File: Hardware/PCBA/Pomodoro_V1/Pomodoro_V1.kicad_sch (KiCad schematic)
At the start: 0 parts

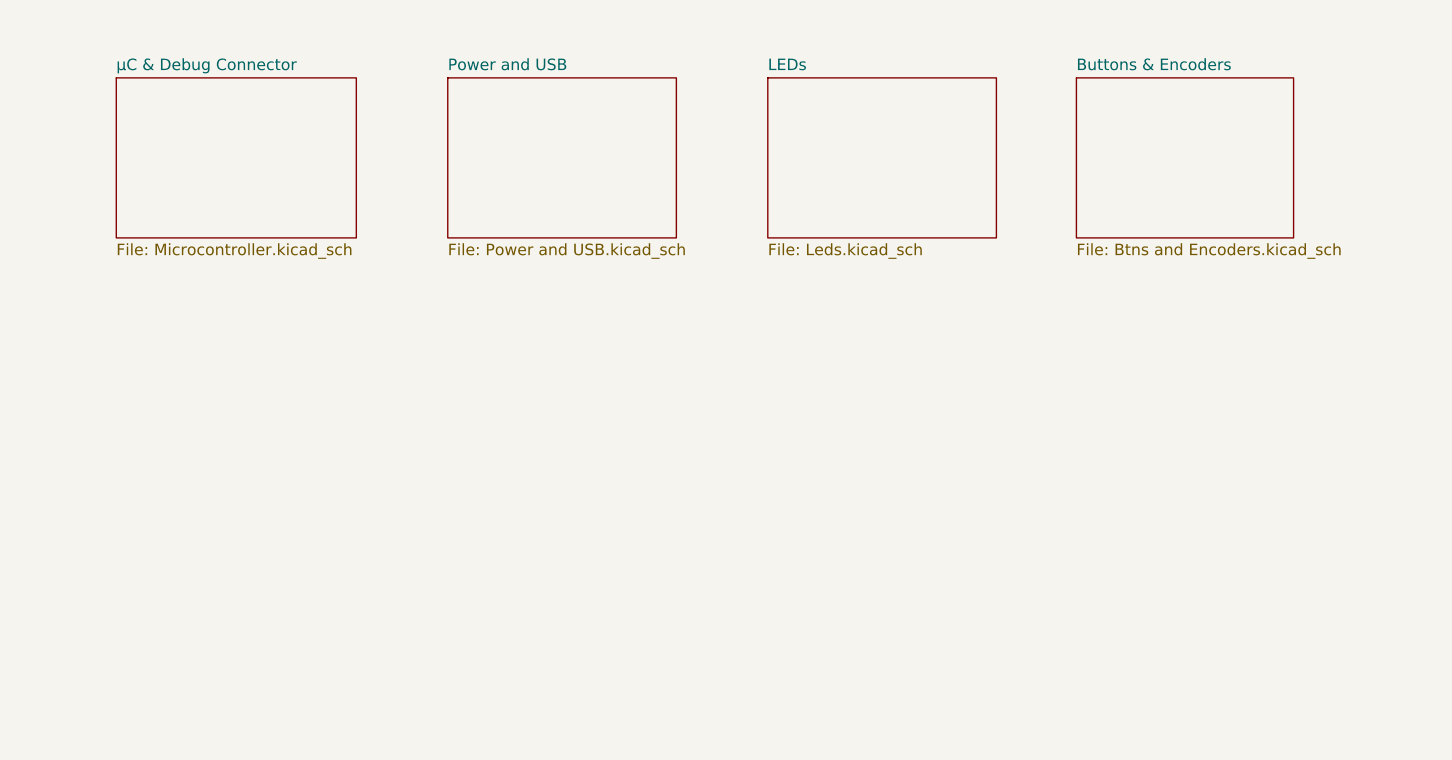
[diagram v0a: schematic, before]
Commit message: Updated CubeMx File, Created Schematic for µC, layouted the LEDs on the PCB
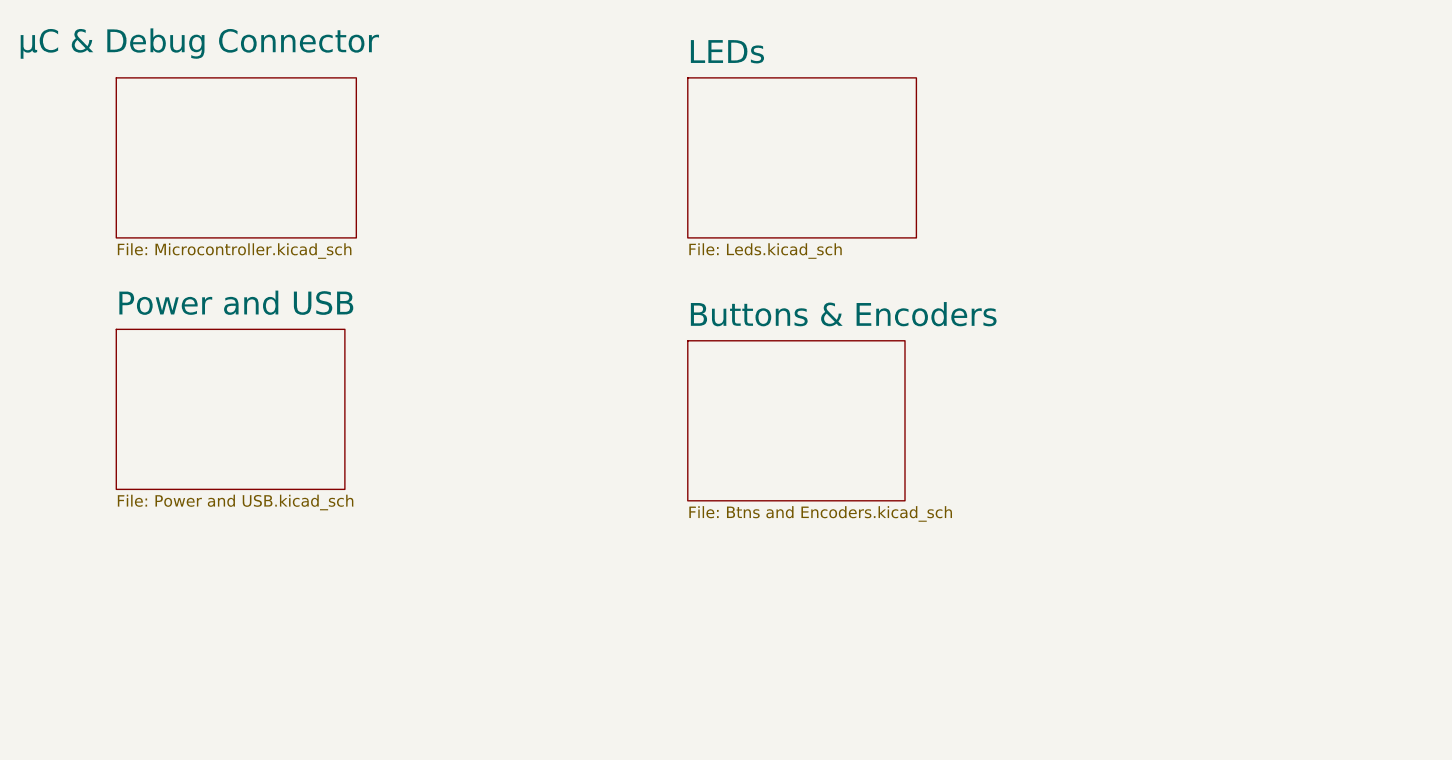
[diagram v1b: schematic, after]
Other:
- company: (none) -> Max Koell (c)
- title: (none) -> Pomodoro_Clock
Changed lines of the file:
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@@
 	(generator_version "8.0")
 	(paper "A4")
+	(title_block
+		(title "Pomodoro_Clock")
+		(date "2024-02-29")
+		(rev "1")
+		(company "Max Koell (c)")
+	)
 	(sheet
-		(at 134.62 63.5)
+		(at 125.73 63.5)
 		(size 25.4 17.78)
 		(fields_autoplaced yes)
@@
 		)
 		(property "Sheetname" "LEDs"
-			(at 134.62 62.7884 0)
+			(at 125.73 62.1534 0)
 			(effects
 				(font
-					(size 1.27 1.27)
+					(size 2.54 2.54)
 				)
 				(justify left bottom)
@@
 		)
 		(property "Sheetfile" "Leds.kicad_sch"
-			(at 134.62 81.8646 0)
+			(at 125.73 81.8646 0)
 			(effects
 				(font
@@
 		(at 62.23 63.5)
 		(size 26.67 17.78)
-		(fields_autoplaced yes)
 		(stroke
 			(width 0.1524)
@@
 		)
 		(property "Sheetname" "µC & Debug Connector"
-			(at 62.23 62.7884 0)
+			(at 51.308 60.96 0)
 			(effects
 				(font
-					(size 1.27 1.27)
+					(size 2.54 2.54)
 				)
 				(justify left bottom)
@@
 	)
 	(sheet
-		(at 168.91 63.5)
+		(at 125.73 92.71)
 		(size 24.13 17.78)
 		(fields_autoplaced yes)
@@
 		)
 		(property "Sheetname" "Buttons & Encoders"
-			(at 168.91 62.7884 0)
+			(at 125.73 91.3634 0)
 			(effects
 				(font
-					(size 1.27 1.27)
+					(size 2.54 2.54)
 				)
 				(justify left bottom)
@@
 		)
 		(property "Sheetfile" "Btns and Encoders.kicad_sch"
-			(at 168.91 81.8646 0)
+			(at 125.73 111.0746 0)
 			(effects
 				(font
@@
 	)
 	(sheet
-		(at 99.06 63.5)
+		(at 62.23 91.44)
 		(size 25.4 17.78)
 		(fields_autoplaced yes)
@@
 		)
 		(property "Sheetname" "Power and USB"
-			(at 99.06 62.7884 0)
+			(at 62.23 90.0934 0)
 			(effects
 				(font
-					(size 1.27 1.27)
+					(size 2.54 2.54)
 				)
 				(justify left bottom)
@@
 		)
 		(property "Sheetfile" "Power and USB.kicad_sch"
-			(at 99.06 81.8646 0)
+			(at 62.23 109.8046 0)
 			(effects
 				(font

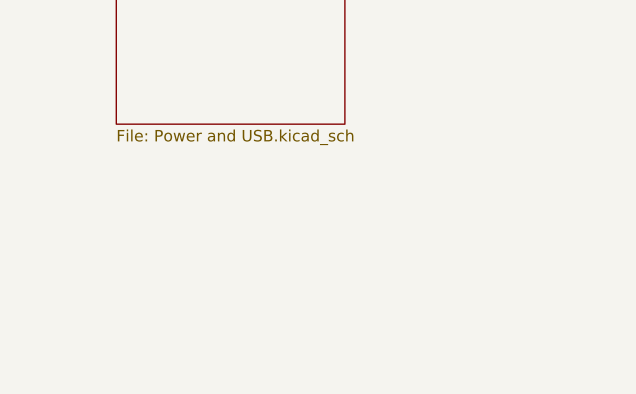
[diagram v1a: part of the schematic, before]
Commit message: added the accelerometer to the Schematic
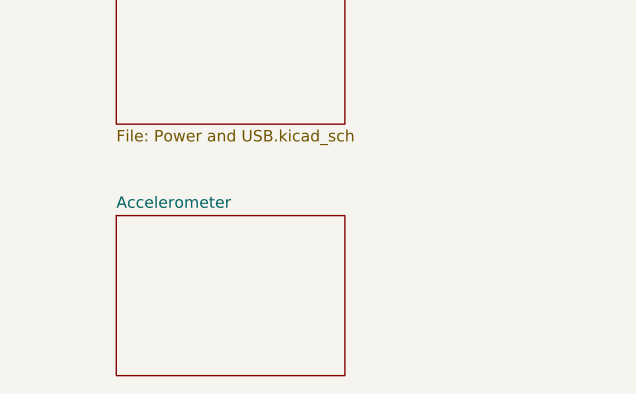
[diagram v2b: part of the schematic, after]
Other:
- added sheet Accelerometer (Accelerometer.kicad_sch)
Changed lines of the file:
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@@
+	)
+	(sheet
+		(at 62.23 119.38)
+		(size 25.4 17.78)
+		(fields_autoplaced yes)
+		(stroke
+			(width 0.1524)
+			(type solid)
+		)
+		(fill
+			(color 0 0 0 0.0000)
+		)
+		(property "Sheetname" "Accelerometer"
+			(at 62.23 118.6684 0)
+			(effects
+				(font
+					(size 1.27 1.27)
+				)
+				(justify left bottom)
+			)
+		)
+		(property "Sheetfile" "Accelerometer.kicad_sch"
+			(at 62.23 137.7446 0)
+			(effects
+				(font
+					(size 1.27 1.27)
+				)
+				(justify left top)
+				(hide yes)
+			)
+		)
+		(instances
+			(project "Pomodoro_V1"
+				(path "/8b8515f0-2a7a-4fc4-bc5a-86877c499298"
+					(page "9")
+				)
+			)
+		)
 	)
 	(sheet

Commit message: Finalized the schematic, First Draft of the finished Layout
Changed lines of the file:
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@@
 		)
 		(property "Sheetname" "µC & Debug Connector"
-			(at 51.308 60.96 0)
+			(at 62.484 60.96 0)
 			(effects
 				(font
@@
 		)
 		(property "Sheetname" "Accelerometer"
-			(at 62.23 118.6684 0)
+			(at 62.23 118.0334 0)
 			(effects
 				(font
-					(size 1.27 1.27)
+					(size 2.54 2.54)
 				)
 				(justify left bottom)
